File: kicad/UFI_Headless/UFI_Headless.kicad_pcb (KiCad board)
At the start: 4 copper layers, 110 x 85 mm, 119 parts, among them J1 USB-C, J2 12V DC 5.5/2.1, J3 FDD_PWR, J4 SWD, J5 DBG_UART, J6 FDD_34PIN, J7 AMIGA_FDD, J8 IEC_HDR, SW1 RESET, SW2 BOOT, U1 USBLC6-2SC6, U10 74LVC14AD, U11 APS6404L-3SQR-SN, U2 TPS54202DDC, U3 TPS2116DRL, U4 AP7361C-33E, U5 STM32H723ZGT6, U6 SN74LS07D, U7 SN74LS07D, U8 74LVC14AD, U9 SN74LS07D, Y1 25MHz CL=12pF

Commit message: UFI Headless v0.4: J6 pin 6 DRATE via JP1, pin 3 GND/+5V via JP2
DRATE is driven by PF11 through the spare LS07 gate U7.11 -> U7.10 with
pull-up RN3.3; J6 pin 6 only sees it when solder jumper JP1 is bridged.
J6 pin 3 goes through JP2 (default 1-2 = GND, 2-3 = FDD_5V for PS/2 drives).
Firmware moves FDD_DRATE from PE6 to PF11.
DRC 0 violations, 0 unconnected, parity clean; fab outputs regenerated.
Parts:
- added JP1: DRATE, Jumper:SolderJumper-2_P1.3mm_Open_RoundedPad1.0x1.5mm, F.Cu at (19.0, 73.4)
- added JP2: PIN3_GND/5V, Jumper:SolderJumper-3_P1.3mm_Bridged12_RoundedPad1.0x1.5mm, F.Cu at (11.5, 73.4)
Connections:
- J6 pad 3: GND -> /FDD_Connectors/FD_PIN3
- J6 pad 6: unconnected-(J6-Pin_6-Pad6) -> /FDD_Connectors/FD_PIN6
- RN3 pad 3: unconnected-(RN3-R3.1-Pad3) -> FD_DRATE
- RN3 pad 6: unconnected-(RN3-R3.2-Pad6) -> +5V
- U5 pad 49: unconnected-(U5-PF11-Pad49) -> FDD_DRATE
- U7 pad 10: unconnected-(U7-Pad10) -> FD_DRATE
- U7 pad 11: +5V -> FDD_DRATE
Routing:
- net FD_DRATE: track 0.00 -> 62.0 mm, vias 0 -> 5
- net FDD_DRATE: track 0.00 -> 27.3 mm, vias 0 -> 2
- net FDD_5V: track 105.5 -> 118.7 mm, vias 3 -> 4
- net /FDD_Connectors/FD_PIN6: track 0.00 -> 9.55 mm
- net /FDD_Connectors/FD_PIN3: track 0.00 -> 8.61 mm
- net +5V: track 248.5 -> 254.4 mm, vias 3 -> 5
- net FD_WPROT: track 93.8 -> 98.3 mm, vias 0 -> 3
- net FD_INDEX: track 121.0 -> 122.0 mm, vias 1 -> 2
- net GND: vias 401 -> 398

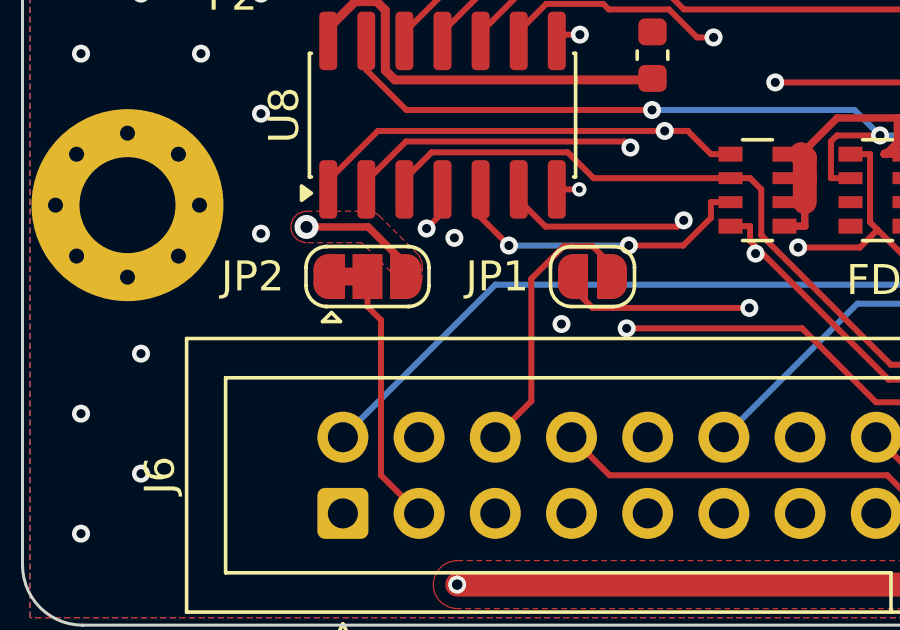
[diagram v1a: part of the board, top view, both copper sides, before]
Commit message: UFI Headless v0.4: silkscreen labels for JP1/JP2
Back side explains both jumpers (JP1 = DRATE on J6 pin 6, JP2 1-2 GND /
2-3 +5V for PS/2 drives only), front marks the +5V side of JP2.
New scripts/add_silk_label.py places a label at the nearest spot free of
pads, vias and silkscreen. DRC 0 / 0 unconnected / parity clean.
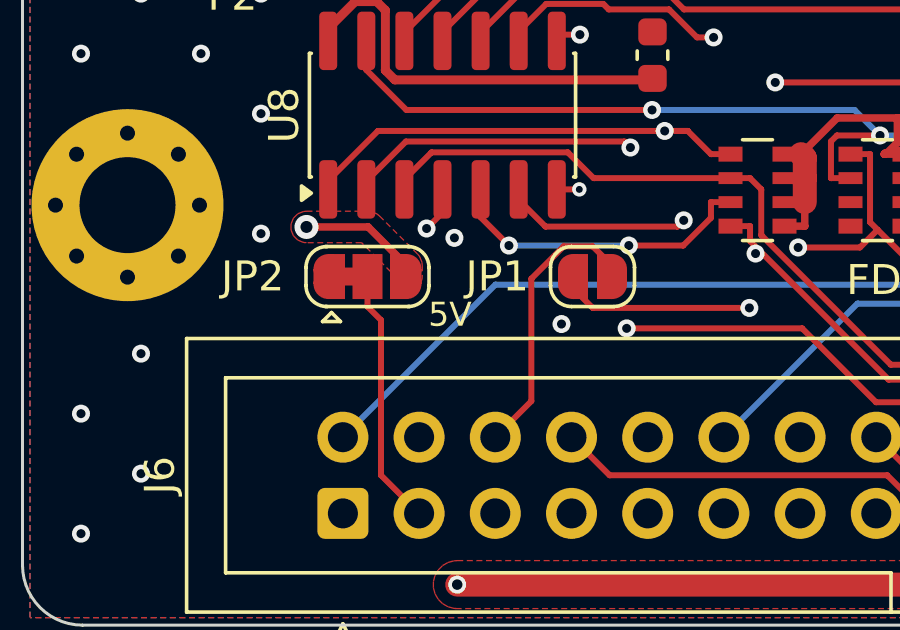
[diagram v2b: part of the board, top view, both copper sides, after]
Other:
- board text added: "5V"
- board text added: "JP1 bridge: J6.6=DRATE"
- board text added: "JP2 1-2 GND / 2-3 +5V (PS/2 only)"
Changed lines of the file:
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@@
+		)
+	)
+	(gr_text "5V"
+		(at 14.25 74.65 0)
+		(layer "F.SilkS")
+		(effects
+			(font
+				(size 0.8 0.8)
+				(thickness 0.12)
+			)
 		)
 	)
@@
 		)
 	)
+	(gr_text "JP2 1-2 GND / 2-3 +5V (PS/2 only)"
+		(at 12.5 76.65 0)
+		(layer "B.SilkS")
+		(effects
+			(font
+				(size 0.8 0.8)
+				(thickness 0.12)
+			)
+			(justify mirror)
+		)
+	)
+	(gr_text "JP1 bridge: J6.6=DRATE"
+		(at 19.25 73.65 0)
+		(layer "B.SilkS")
+		(effects
+			(font
+				(size 0.8 0.8)
+				(thickness 0.12)
+			)
+			(justify mirror)
+		)
+	)

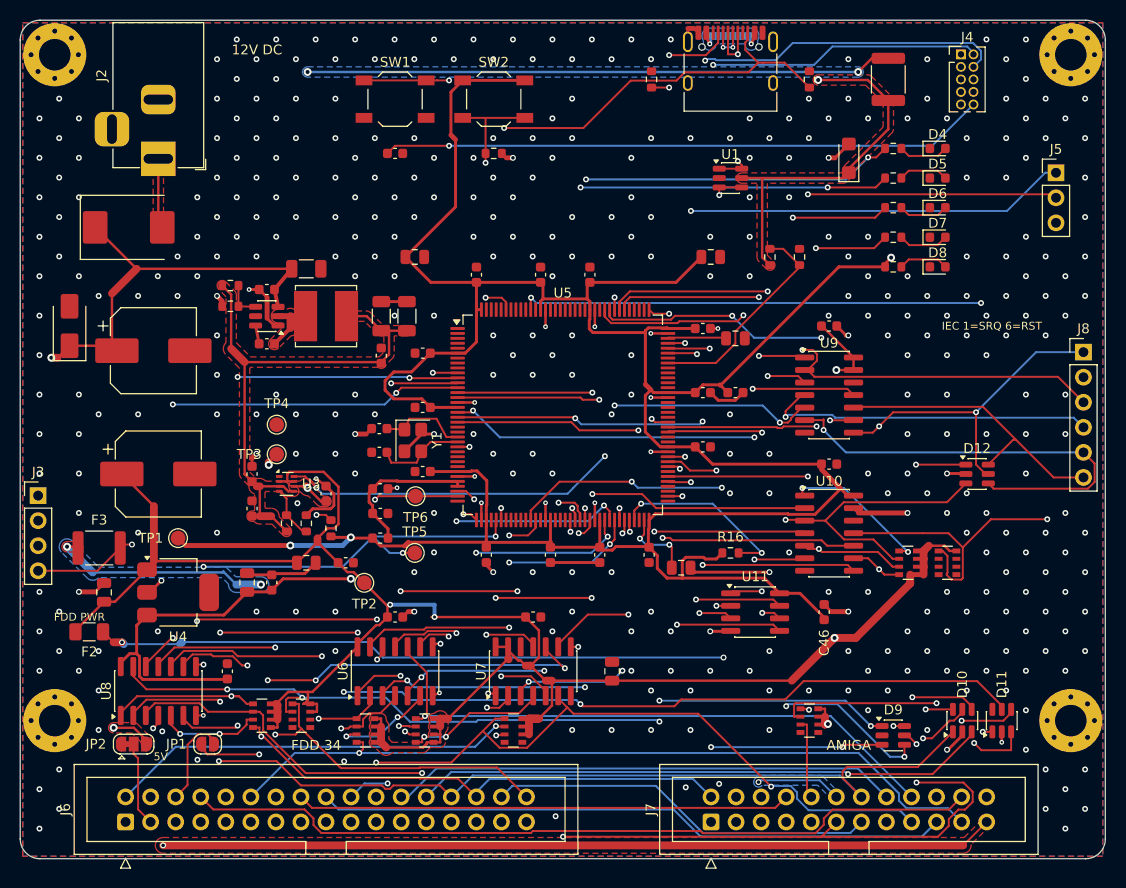
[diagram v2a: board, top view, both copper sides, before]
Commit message: UFI Headless v0.5: switched/measured drive supplies, write lock, microSD, expansion
Hardware (A1-A9): FDD_5V/FDD_12V high-side P-FET switches (off in reset)
with 0.1R + INA180A1 current sense, TVS at both outputs; WRITE LOCK
jumper J11 gates WGATE through 74LVC1G32 (TP8 now shows the gated
signal); expansion header J9 (I2C1, 2 GPIO, button lines, 3V3/5V),
buttons SW3/SW4; microSD J10 on SDMMC2 with the card slot facing the
top edge; board ID divider on PA4; test points TP7/TP8.  12V reverse
protection already existed; 8-inch 50-pin port left out (board size).
ECO placed 37 parts; Freerouting plus hand routes for the rest.
New scripts/eco/ tools (maze router, route check, cluster/occupancy
maps, via scan), add_silk_label.py no longer crashes on re-placement.
ERC 0, DRC 0 incl. warnings, 0 unconnected, parity clean, no via-in-pad;
fab outputs regenerated (146 CPL rows).
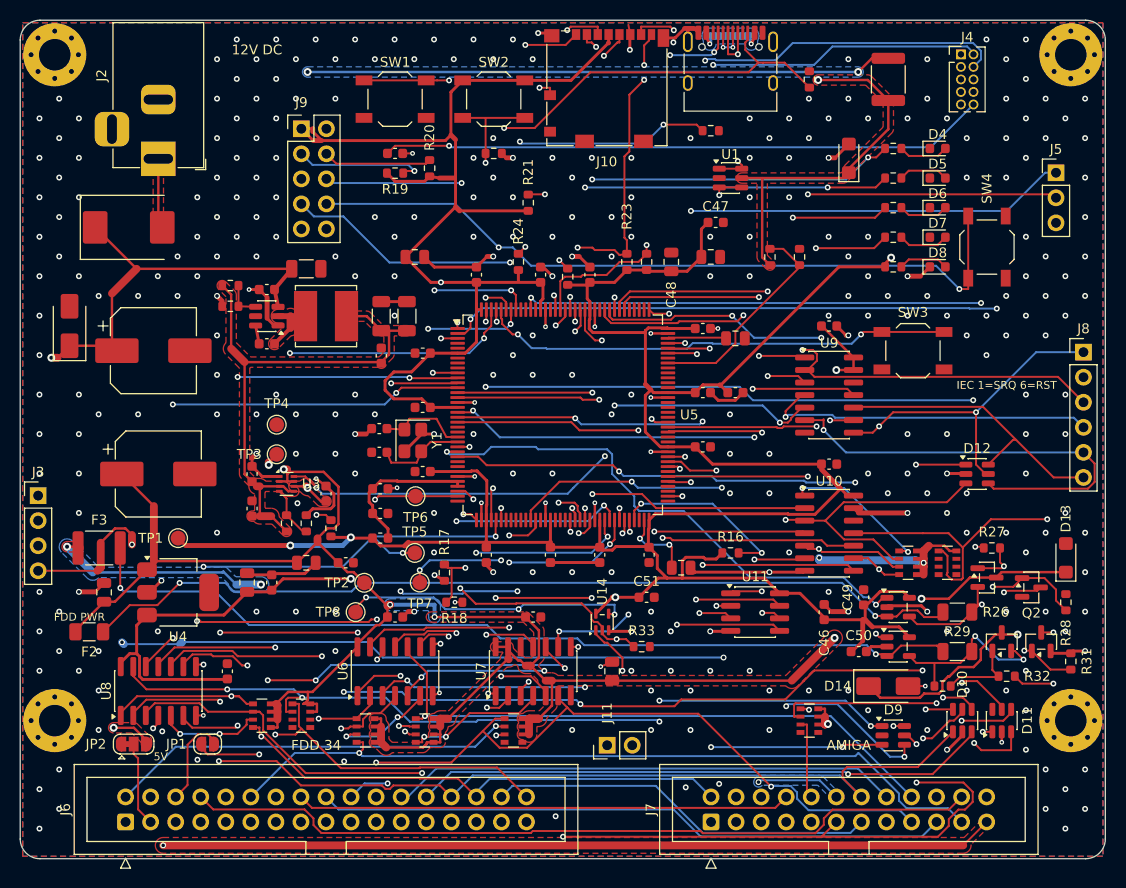
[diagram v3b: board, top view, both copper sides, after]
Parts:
- added C47: 100nF, Capacitor_SMD:C_0603_1608Metric, F.Cu at (70.5, 20.5)
- added C48: 10uF, Capacitor_SMD:C_0805_2012Metric, F.Cu at (66.0, 24.5)
- added C49: 100nF, Capacitor_SMD:C_0603_1608Metric, F.Cu at (85.5, 58.5)
- added C50: 100nF, Capacitor_SMD:C_0603_1608Metric, F.Cu at (85.0, 64.0)
- added C51: 100nF, Capacitor_SMD:C_0603_1608Metric, F.Cu at (63.5, 58.5)
- added D13: SMF5.0CA, Diode_SMD:D_SMF, F.Cu at (106.0, 54.5)
- added D14: SMAJ15CA, Diode_SMD:D_SMA, F.Cu at (88.0, 67.5)
- added J10: 104031-0811, Connector_Card:microSD_HC_Molex_104031-0811, F.Cu at (59.5, 6.90)
- added J11: WRITE_LOCK, Connector_PinHeader_2.54mm:PinHeader_1x02_P2.54mm_Vertical, F.Cu at (59.5, 73.5)
- added J9: EXPANSION, Connector_PinHeader_2.54mm:PinHeader_2x05_P2.54mm_Vertical, F.Cu at (28.5, 11.0)
- added Q1: AO3401A, Package_TO_SOT_SMD:SOT-23, F.Cu at (98.0, 56.5)
- added Q2: 2N7002, Package_TO_SOT_SMD:SOT-23, F.Cu at (102.5, 57.5)
- added Q3: AO3401A, Package_TO_SOT_SMD:SOT-23, F.Cu at (99.5, 63.0)
- added Q4: 2N7002, Package_TO_SOT_SMD:SOT-23, F.Cu at (103.5, 63.0)
- added R17: 10k, Resistor_SMD:R_0603_1608Metric, F.Cu at (43.0, 56.0)
- added R18: 10k, Resistor_SMD:R_0603_1608Metric, F.Cu at (44.0, 59.0)
- added R19: 2.2k, Resistor_SMD:R_0603_1608Metric, F.Cu at (38.0, 15.5)
- added R20: 2.2k, Resistor_SMD:R_0603_1608Metric, F.Cu at (41.5, 15.0)
- added R21: 47k, Resistor_SMD:R_0603_1608Metric, F.Cu at (51.5, 18.5)
- added R22: 47k, Resistor_SMD:R_0603_1608Metric, F.Cu at (55.5, 26.0)
- added R23: 47k, Resistor_SMD:R_0603_1608Metric, F.Cu at (61.5, 24.5)
- added R24: 47k, Resistor_SMD:R_0603_1608Metric, F.Cu at (50.5, 24.5)
- added R25: 47k, Resistor_SMD:R_0603_1608Metric, F.Cu at (63.5, 24.5)
- added R26: 0.1R 1%, Resistor_SMD:R_1206_3216Metric, F.Cu at (95.0, 60.0)
- added R27: 100k, Resistor_SMD:R_0603_1608Metric, F.Cu at (98.5, 53.5)
- added R28: 100k, Resistor_SMD:R_0603_1608Metric, F.Cu at (106.0, 59.0)
- added R29: 0.1R 1%, Resistor_SMD:R_1206_3216Metric, F.Cu at (95.0, 64.0)
- added R30: 10k, Resistor_SMD:R_0603_1608Metric, F.Cu at (93.5, 67.5)
- added R31: 100k, Resistor_SMD:R_0603_1608Metric, F.Cu at (106.5, 65.0)
- added R32: 10k, Resistor_SMD:R_0603_1608Metric, F.Cu at (100.0, 66.5)
- added R33: 100k, Resistor_SMD:R_0603_1608Metric, F.Cu at (63.0, 63.5)
- added SW3: BTN_A, Button_Switch_SMD:SW_SPST_TL3342, F.Cu at (90.5, 33.5)
- added SW4: BTN_B, Button_Switch_SMD:SW_SPST_TL3342, F.Cu at (98.0, 23.0)
- added TP7: TP_WDATA, TestPoint:TestPoint_Pad_D1.5mm, F.Cu at (40.5, 57.0)
- added TP8: TP_WGATE, TestPoint:TestPoint_Pad_D1.5mm, F.Cu at (34.0, 60.0)
- added U12: INA180A1, Package_TO_SOT_SMD:SOT-23-5, F.Cu at (89.0, 59.5)
- added U13: INA180A1, Package_TO_SOT_SMD:SOT-23-5, F.Cu at (89.0, 63.5)
- added U14: 74LVC1G32GW, Package_TO_SOT_SMD:SOT-353_SC-70-5, F.Cu at (59.0, 61.0)
- moved R1 7.94 mm to (70.0, 11.2), turned to 0 degrees
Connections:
- F2 pad 2: FDD_5V -> /Power/FDD5_F
- F3 pad 2: FDD_12V -> /Power/FDD12_F
- U5 pad 1: unconnected-(U5-PE2-Pad1) -> FDD5_EN
- U5 pad 122: unconnected-(U5-PD6-Pad122) -> /MCU_Core/SD_CLK
- U5 pad 123: unconnected-(U5-PD7-Pad123) -> /MCU_Core/SD_CMD
- U5 pad 124: unconnected-(U5-PG9-Pad124) -> /MCU_Core/SD_D0
- U5 pad 125: unconnected-(U5-PG10-Pad125) -> /MCU_Core/SD_D1
- U5 pad 126: unconnected-(U5-PG11-Pad126) -> /MCU_Core/SD_D2
- U5 pad 127: unconnected-(U5-PG12-Pad127) -> /MCU_Core/SD_D3
- U5 pad 128: unconnected-(U5-PG13-Pad128) -> /MCU_Core/SD_CD
- U5 pad 136: unconnected-(U5-PB6-Pad136) -> /MCU_Core/I2C_SCL
- U5 pad 137: unconnected-(U5-PB7-Pad137) -> /MCU_Core/I2C_SDA
- U5 pad 139: unconnected-(U5-PB8-Pad139) -> /MCU_Core/BTN_A
- U5 pad 140: unconnected-(U5-PB9-Pad140) -> /MCU_Core/BTN_B
- U5 pad 141: unconnected-(U5-PE0-Pad141) -> /MCU_Core/EXP_IO1
- U5 pad 142: unconnected-(U5-PE1-Pad142) -> /MCU_Core/EXP_IO2
- U5 pad 2: unconnected-(U5-PE3-Pad2) -> FDD12_EN
- U5 pad 26: unconnected-(U5-PC0-Pad26) -> I_FDD5
- U5 pad 27: unconnected-(U5-PC1-Pad27) -> I_FDD12
- U5 pad 3: unconnected-(U5-PE4-Pad3) -> WLOCK
- U5 pad 40: unconnected-(U5-PA4-Pad40) -> /MCU_Core/BOARD_ID
- U7 pad 3: FDD_WGATE -> FDD_WGATE_G
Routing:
- net FDD12_EN: track 0.00 -> 97.6 mm, vias 0 -> 3
- net +3V3: track 359.9 -> 451.2 mm, vias 4 -> 7
- net /Power/FDD12_F: track 0.00 -> 91.0 mm, vias 0 -> 2
- net /Power/FDD5_F: track 0.00 -> 90.1 mm, vias 0 -> 2
- net FDD5_EN: track 0.00 -> 87.9 mm, vias 0 -> 4
- net /MCU_Core/BTN_B: track 0.00 -> 84.9 mm, vias 0 -> 3
- net /MCU_Core/BTN_A: track 0.00 -> 79.3 mm, vias 0 -> 3
- net WLOCK: track 0.00 -> 60.1 mm, vias 0 -> 3
- net I_FDD12: track 0.00 -> 58.9 mm, vias 0 -> 3
- net I_FDD5: track 0.00 -> 54.8 mm, vias 0 -> 2
- net +5V: track 254.4 -> 306.1 mm, vias 5 -> 8
- net /MCU_Core/SD_D0: track 0.00 -> 46.0 mm, vias 0 -> 3
- net GND: track 102.0 -> 146.9 mm, vias 398 -> 323
- net FDD_12V: track 126.9 -> 170.1 mm, vias 2 -> 3
- net /MCU_Core/I2C_SDA: track 0.00 -> 43.1 mm, vias 0 -> 2
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- added copper zone on B.Cu, net +5V
